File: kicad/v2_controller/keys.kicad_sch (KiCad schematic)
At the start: 34 parts

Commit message: [kicad] additional work on v2 controller
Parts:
- SW1: renamed from SW18; footprint (none) -> mantyl:Kailh_socket_MX_platemount
- SW10: renamed from SW7; footprint (none) -> mantyl:Kailh_socket_MX_platemount
- SW11: renamed from SW8; footprint (none) -> mantyl:Kailh_socket_MX_platemount
- SW12: renamed from SW9; footprint (none) -> mantyl:Kailh_socket_MX_platemount
- SW13: renamed from SW10; footprint (none) -> mantyl:Kailh_socket_MX_platemount
- SW14: renamed from SW3; footprint (none) -> mantyl:Kailh_socket_MX_platemount
- SW15: renamed from SW4; footprint (none) -> mantyl:Kailh_socket_MX_platemount
- SW16: renamed from SW5; footprint (none) -> mantyl:Kailh_socket_MX_platemount
- SW17: renamed from SW6; footprint (none) -> mantyl:Kailh_socket_MX_platemount
- SW2: renamed from SW19; footprint (none) -> mantyl:Kailh_socket_MX_platemount
- SW3: renamed from SW14; footprint (none) -> mantyl:Kailh_socket_MX_platemount
- SW4: renamed from SW15; footprint (none) -> mantyl:Kailh_socket_MX_platemount
- SW5: renamed from SW16; footprint (none) -> mantyl:Kailh_socket_MX_platemount
- SW6: renamed from SW17; footprint (none) -> mantyl:Kailh_socket_MX_platemount
- SW7: renamed from SW11; footprint (none) -> mantyl:Kailh_socket_MX_platemount
- SW8: renamed from SW12; footprint (none) -> mantyl:Kailh_socket_MX_platemount
- SW9: renamed from SW13; footprint (none) -> mantyl:Kailh_socket_MX_platemount
- renumbered D4 to D21, D8 to D22, D12 to D23, D15 to D24, D19 to D25, D5 to D26, D9 to D27, D13 to D28, D16 to D29, D6 to D30, D10 to D31, D14 to D32, D17 to D33, D20 to D34, D7 to D35, D11 to D36, D18 to D37
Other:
- note added: "Key Switches"

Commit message: [kicad] fix global symbol usage in v2 controller
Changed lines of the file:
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@@
     (effects (font (size 5 5) (thickness 1) bold (color 194 0 0 1)) (justify left bottom))
   )
-  (label "ROW6" (at 31.75 124.46 180) (fields_autoplaced)
-    (effects (font (size 1.27 1.27)) (justify right bottom))
+  (global_label "ROW5" (shape input) (at 31.75 95.25 180) (fields_autoplaced)
+    (effects (font (size 1.27 1.27)) (justify right))
+    (property "Intersheetrefs" "${INTERSHEET_REFS}" (at 23.5034 95.25 0)
+      (effects (font (size 1.27 1.27)) (justify right) hide)
+    )
   )
-  (label "ROW2" (at 31.75 60.96 180) (fields_autoplaced)
-    (effects (font (size 1.27 1.27)) (justify right bottom))
+  (global_label "COL8" (shape input) (at 38.1 190.5 0) (fields_autoplaced)
+    (effects (font (size 1.27 1.27)) (justify left))
+    (property "Intersheetrefs" "${INTERSHEET_REFS}" (at 45.9233 190.5 0)
+      (effects (font (size 1.27 1.27)) (justify left) hide)
+    )
   )
-  (label "ROW7" (at 31.75 127 180) (fields_autoplaced)
-    (effects (font (size 1.27 1.27)) (justify right bottom))
+  (global_label "ROW2" (shape input) (at 31.75 60.96 180) (fields_autoplaced)
+    (effects (font (size 1.27 1.27)) (justify right))
+    (property "Intersheetrefs" "${INTERSHEET_REFS}" (at 23.5034 60.96 0)
+      (effects (font (size 1.27 1.27)) (justify right) hide)
+    )
   )
-  (label "COL8" (at 38.1 190.5 0) (fields_autoplaced)
-    (effects (font (size 1.27 1.27)) (justify left bottom))
+  (global_label "ROW0" (shape input) (at 31.75 29.21 180) (fields_autoplaced)
+    (effects (font (size 1.27 1.27)) (justify right))
+    (property "Intersheetrefs" "${INTERSHEET_REFS}" (at 23.5034 29.21 0)
+      (effects (font (size 1.27 1.27)) (justify right) hide)
+    )
   )
-  (label "ROW3" (at 31.75 63.5 180) (fields_autoplaced)
-    (effects (font (size 1.27 1.27)) (justify right bottom))
+  (global_label "ROW1" (shape input) (at 31.75 31.75 180) (fields_autoplaced)
+    (effects (font (size 1.27 1.27)) (justify right))
+    (property "Intersheetrefs" "${INTERSHEET_REFS}" (at 23.5034 31.75 0)
+      (effects (font (size 1.27 1.27)) (justify right) hide)
+    )
   )
-  (label "ROW4" (at 31.75 92.71 180) (fields_autoplaced)
-    (effects (font (size 1.27 1.27)) (justify right bottom))
+  (global_label "ROW7" (shape input) (at 31.75 127 180) (fields_autoplaced)
+    (effects (font (size 1.27 1.27)) (justify right))
+    (property "Intersheetrefs" "${INTERSHEET_REFS}" (at 23.5034 127 0)
+      (effects (font (size 1.27 1.27)) (justify right) hide)
+    )
   )
-  (label "ROW5" (at 31.75 95.25 180) (fields_autoplaced)
-    (effects (font (size 1.27 1.27)) (justify right bottom))
+  (global_label "ROW3" (shape input) (at 31.75 63.5 180) (fields_autoplaced)
+    (effects (font (size 1.27 1.27)) (justify right))
+    (property "Intersheetrefs" "${INTERSHEET_REFS}" (at 23.5034 63.5 0)
+      (effects (font (size 1.27 1.27)) (justify right) hide)
+    )
   )
-  (label "COL9" (at 101.6 190.5 0) (fields_autoplaced)
-    (effects (font (size 1.27 1.27)) (justify left bottom))
+  (global_label "ROW8" (shape input) (at 31.75 158.75 180) (fields_autoplaced)
+    (effects (font (size 1.27 1.27)) (justify right))
+    (property "Intersheetrefs" "${INTERSHEET_REFS}" (at 23.5034 158.75 0)
+      (effects (font (size 1.27 1.27)) (justify right) hide)
+    )
   )
-  (label "ROW0" (at 31.75 29.21 180) (fields_autoplaced)
-    (effects (font (size 1.27 1.27)) (justify right bottom))
+  (global_label "ROW6" (shape input) (at 31.75 124.46 180) (fields_autoplaced)
+    (effects (font (size 1.27 1.27)) (justify right))
+    (property "Intersheetrefs" "${INTERSHEET_REFS}" (at 23.5034 124.46 0)
+      (effects (font (size 1.27 1.27)) (justify right) hide)
+    )
   )
-  (label "ROW8" (at 31.75 158.75 180) (fields_autoplaced)
-    (effects (font (size 1.27 1.27)) (justify right bottom))
+  (global_label "COL9" (shape input) (at 101.6 190.5 0) (fields_autoplaced)
+    (effects (font (size 1.27 1.27)) (justify left))
+    (property "Intersheetrefs" "${INTERSHEET_REFS}" (at 109.4233 190.5 0)
+      (effects (font (size 1.27 1.27)) (justify left) hide)
+    )
   )
-  (label "ROW1" (at 31.75 31.75 180) (fields_autoplaced)
-    (effects (font (size 1.27 1.27)) (justify right bottom))
+  (global_label "ROW4" (shape input) (at 31.75 92.71 180) (fields_autoplaced)
+    (effects (font (size 1.27 1.27)) (justify right))
+    (property "Intersheetrefs" "${INTERSHEET_REFS}" (at 23.5034 92.71 0)
+      (effects (font (size 1.27 1.27)) (justify right) hide)
+    )
   )
   (symbol (lib_id "mantyl:Kailh_MX_Socket") (at 149.225 67.31 0) (unit 1)

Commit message: [kicad] update v2 controller to use hierarchical labels
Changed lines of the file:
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@@
     (effects (font (size 5 5) (thickness 1) bold (color 194 0 0 1)) (justify left bottom))
   )
-  (global_label "ROW5" (shape input) (at 31.75 95.25 180) (fields_autoplaced)
+  (label "ROW5" (at 31.75 95.25 180) (fields_autoplaced)
     (effects (font (size 1.27 1.27)) (justify right))
     (property "Intersheetrefs" "${INTERSHEET_REFS}" (at 23.5034 95.25 0)
@@
     )
   )
-  (global_label "COL8" (shape input) (at 38.1 190.5 0) (fields_autoplaced)
+  (label "COL8" (at 38.1 190.5 0) (fields_autoplaced)
     (effects (font (size 1.27 1.27)) (justify left))
     (property "Intersheetrefs" "${INTERSHEET_REFS}" (at 45.9233 190.5 0)
@@
     )
   )
-  (global_label "ROW2" (shape input) (at 31.75 60.96 180) (fields_autoplaced)
+  (label "ROW2" (at 31.75 60.96 180) (fields_autoplaced)
     (effects (font (size 1.27 1.27)) (justify right))
     (property "Intersheetrefs" "${INTERSHEET_REFS}" (at 23.5034 60.96 0)
@@
     )
   )
-  (global_label "ROW0" (shape input) (at 31.75 29.21 180) (fields_autoplaced)
+  (label "ROW0" (at 31.75 29.21 180) (fields_autoplaced)
     (effects (font (size 1.27 1.27)) (justify right))
     (property "Intersheetrefs" "${INTERSHEET_REFS}" (at 23.5034 29.21 0)
@@
     )
   )
-  (global_label "ROW1" (shape input) (at 31.75 31.75 180) (fields_autoplaced)
+  (label "ROW1" (at 31.75 31.75 180) (fields_autoplaced)
     (effects (font (size 1.27 1.27)) (justify right))
     (property "Intersheetrefs" "${INTERSHEET_REFS}" (at 23.5034 31.75 0)
@@
     )
   )
-  (global_label "ROW7" (shape input) (at 31.75 127 180) (fields_autoplaced)
+  (label "ROW7" (at 31.75 127 180) (fields_autoplaced)
     (effects (font (size 1.27 1.27)) (justify right))
     (property "Intersheetrefs" "${INTERSHEET_REFS}" (at 23.5034 127 0)
@@
     )
   )
-  (global_label "ROW3" (shape input) (at 31.75 63.5 180) (fields_autoplaced)
+  (label "ROW3" (at 31.75 63.5 180) (fields_autoplaced)
     (effects (font (size 1.27 1.27)) (justify right))
     (property "Intersheetrefs" "${INTERSHEET_REFS}" (at 23.5034 63.5 0)
@@
     )
   )
-  (global_label "ROW8" (shape input) (at 31.75 158.75 180) (fields_autoplaced)
+  (label "ROW8" (at 31.75 158.75 180) (fields_autoplaced)
     (effects (font (size 1.27 1.27)) (justify right))
     (property "Intersheetrefs" "${INTERSHEET_REFS}" (at 23.5034 158.75 0)
@@
     )
   )
-  (global_label "ROW6" (shape input) (at 31.75 124.46 180) (fields_autoplaced)
+  (label "ROW6" (at 31.75 124.46 180) (fields_autoplaced)
     (effects (font (size 1.27 1.27)) (justify right))
     (property "Intersheetrefs" "${INTERSHEET_REFS}" (at 23.5034 124.46 0)
@@
     )
   )
-  (global_label "COL9" (shape input) (at 101.6 190.5 0) (fields_autoplaced)
+  (label "COL9" (at 101.6 190.5 0) (fields_autoplaced)
     (effects (font (size 1.27 1.27)) (justify left))
     (property "Intersheetrefs" "${INTERSHEET_REFS}" (at 109.4233 190.5 0)
@@
     )
   )
-  (global_label "ROW4" (shape input) (at 31.75 92.71 180) (fields_autoplaced)
+  (label "ROW4" (at 31.75 92.71 180) (fields_autoplaced)
     (effects (font (size 1.27 1.27)) (justify right))
     (property "Intersheetrefs" "${INTERSHEET_REFS}" (at 23.5034 92.71 0)
@@
     )
   )
+  (hierarchical_label "COL[8..9]" (shape input) (at 209.55 95.25 0) (fields_autoplaced)
+    (effects (font (size 1.27 1.27)) (justify left))
+  )
+  (hierarchical_label "ROW[0..8]" (shape input) (at 209.55 88.9 0) (fields_autoplaced)
+    (effects (font (size 1.27 1.27)) (justify left))
+  )
   (symbol (lib_id "mantyl:Kailh_MX_Socket") (at 149.225 67.31 0) (unit 1)

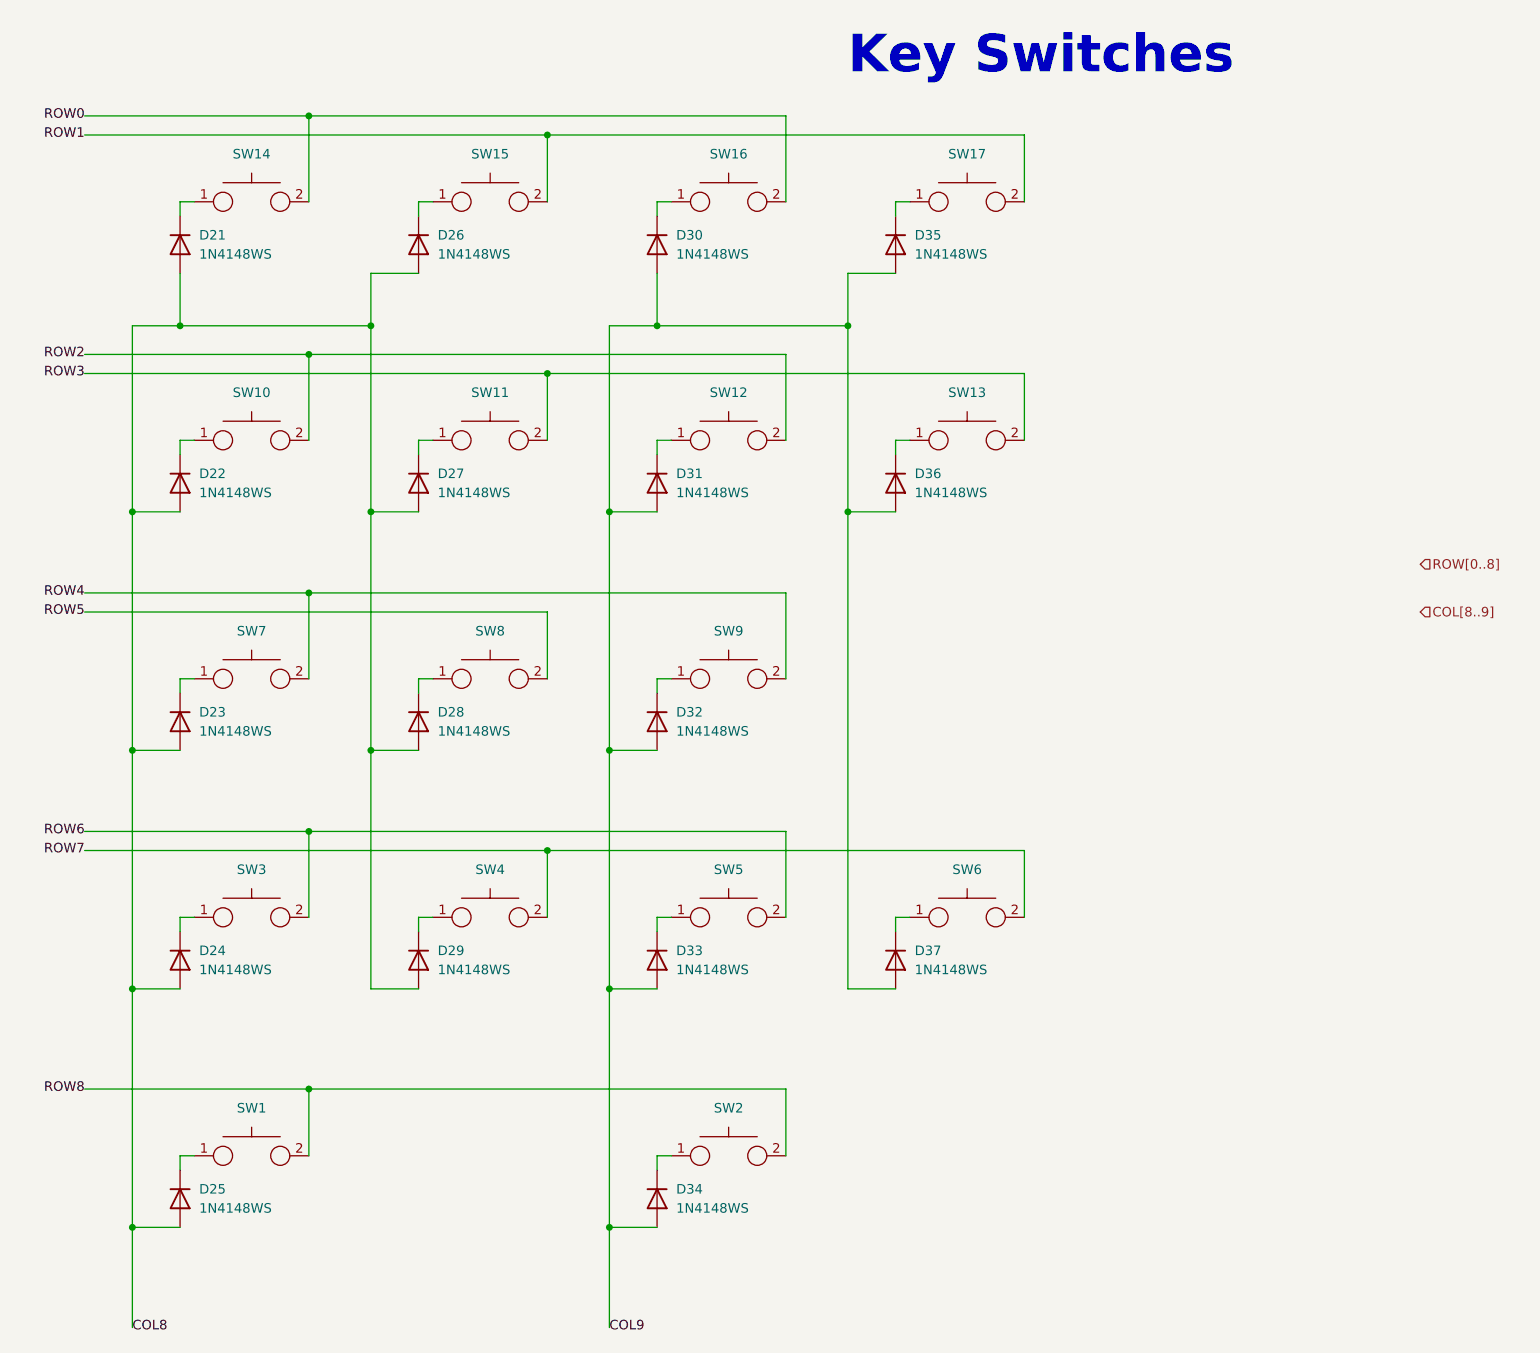
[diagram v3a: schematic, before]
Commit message: [kicad] renumber key diodes, and clean up column wiring
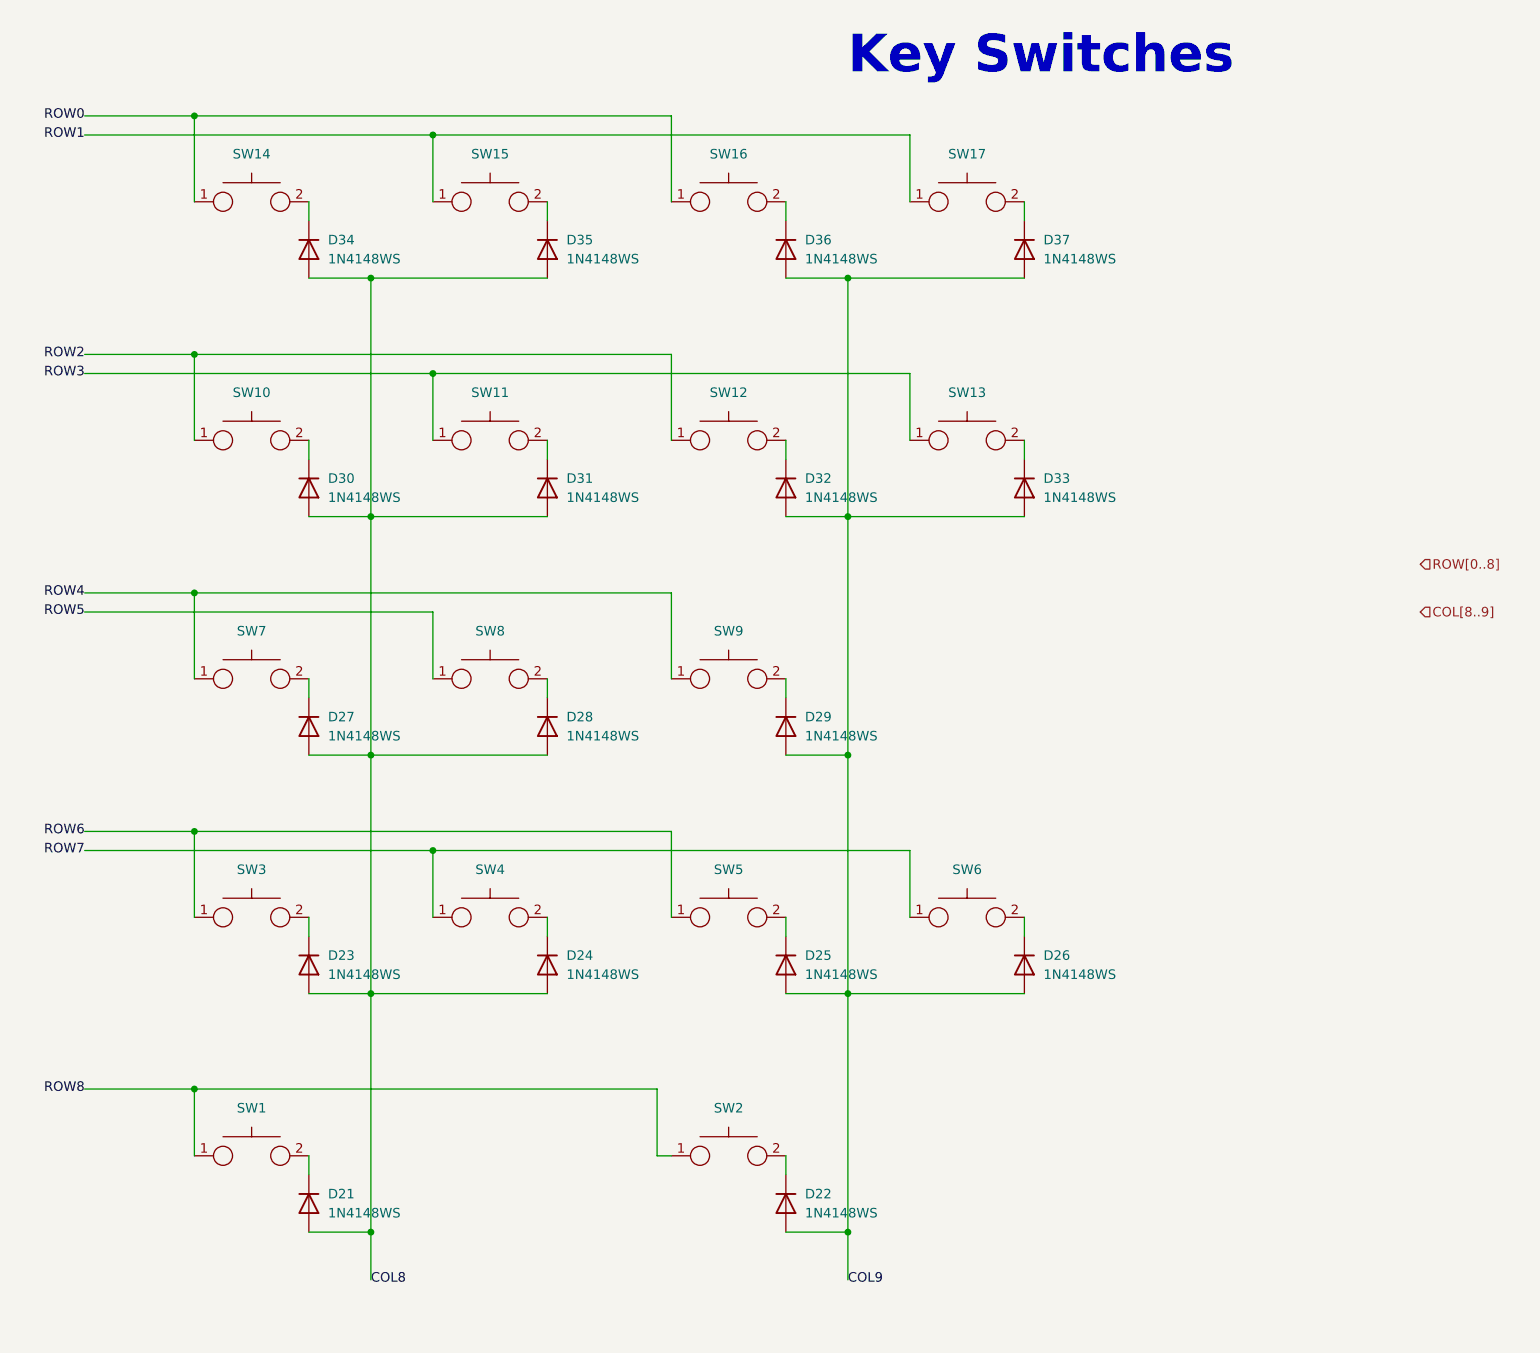
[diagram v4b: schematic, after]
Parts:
- renumbered D25 to D21, D34 to D22, D24 to D23, D29 to D24, D33 to D25, D37 to D26, D23 to D27, D32 to D29, D22 to D30, D27 to D31, D31 to D32, D36 to D33, D21 to D34, D26 to D35, D30 to D36, D35 to D37
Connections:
- net ROW0: now also SW14.1, SW16.1; no longer SW14.2, SW16.2
- net ROW1: now also SW15.1, SW17.1; no longer SW15.2, SW17.2
- net ROW2: now also SW10.1, SW12.1; no longer SW10.2, SW12.2
- net ROW3: now also SW11.1, SW13.1; no longer SW11.2, SW13.2
- net ROW4: now also SW7.1, SW9.1; no longer SW7.2, SW9.2
- net ROW5: now also SW8.1; no longer SW8.2
- net ROW6: now also SW3.1, SW5.1; no longer SW3.2, SW5.2
- net ROW7: now also SW4.1, SW6.1; no longer SW4.2, SW6.2
- net ROW8: now also SW1.1, SW2.1; no longer SW1.2, SW2.2
- net at D33.1 (K): now also SW13.2; no longer SW13.1
- net at D27.1 (K): now also SW7.2; no longer SW7.1
- net at D29.1 (K): now also SW9.2; no longer SW9.1
- net at D24.1 (K): now also SW4.2; no longer SW4.1
- net at D36.1 (K): now also SW16.2; no longer SW16.1
- net at D35.1 (K): now also SW15.2; no longer SW15.1
- net at D22.1 (K): now also SW2.2; no longer SW2.1
- net at D25.1 (K): now also SW5.2; no longer SW5.1
- net at D23.1 (K): now also SW3.2; no longer SW3.1
- net at D37.1 (K): now also SW17.2; no longer SW17.1
- net at D32.1 (K): now also SW12.2; no longer SW12.1
- net at D34.1 (K): now also SW14.2; no longer SW14.1
- net at D21.1 (K): now also SW1.2; no longer SW1.1
- net at D31.1 (K): now also SW11.2; no longer SW11.1
- net at D30.1 (K): now also SW10.2; no longer SW10.1
- net at D26.1 (K): now also SW6.2; no longer SW6.1
- net at D28.1 (K): now also SW8.2; no longer SW8.1
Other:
- moved on the sheet: D21, D22, D23, D24, D25, D26, D27, D28, D29, D30, D31, D32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
